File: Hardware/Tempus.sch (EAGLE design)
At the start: 36 parts, among them J7 AVR_SPI_PRG_6NS, U1 ATMEGA328P_TQFP, Y1 16MHZ

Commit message: Hardware modifications
Hardware modifications
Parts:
- removed J1, J10, J11, J12, J13, J14, J15, J17, J18, J19, J2, J20, J21, J22, J23, J24, J25, J3, J4, J5, J6, J8, J9: (no value), SparkFun-Connectors:M01NOSILK-KIT
- removed J16: (no value), SparkFun-Connectors:M06NO_SILK_FEMALE_PTH
- added U$1: DISP_TFT18, KarlVaello-Displays:DISP_TFT18
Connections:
- net A0: no longer J1.1
- net A1: no longer J2.1
- net A2: no longer J3.1
- net A3: no longer J17.1
- net A4: no longer J20.1
- net A5: no longer J21.1
- net A6: no longer J18.1
- net A7: no longer J19.1
- net D10: no longer J6.1
- net D2: no longer J11.1
- net D3: no longer J12.1
- net D4: no longer J13.1
- net D5: no longer J14.1
- net D6: no longer J15.1
- net D7: no longer J8.1
- net D8: no longer J4.1
- net D9: no longer J5.1
- net DTR: no longer J16.1
- net GND: no longer J16.5, J16.6, J24.1, J25.1
- net RXI: no longer J16.3, J9.1
- net TXO: no longer J10.1, J16.2
- net VCC: no longer J16.4, J22.1, J23.1

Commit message: Hardware modifications
Hardware modifications
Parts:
- removed J7: AVR_SPI_PRG_6NS, SparkFun-Connectors:AVR_SPI_PRG_6NS
- added J1: AVR_SPI_PRG_6TESTPOINTS, SparkFun-Connectors:AVR_SPI_PRG_6TESTPOINTS
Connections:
- net GND: now also J1.6; no longer J7.6
- net MISO: now also J1.1; no longer J7.1
- net MOSI: now also J1.4; no longer J7.4
- net RST: now also J1.5; no longer J7.5
- net SCK: now also J1.3; no longer J7.3
- net VCC: now also J1.2; no longer J7.2
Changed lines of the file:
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@@
 <part name="P+5" library="KarlVaello-Simbols" deviceset="VCC" device=""/>
 <part name="S1" library="SparkFun-Retired" deviceset="TAC_SWITCH" device="SMD" value="RESET"/>
-<part name="J7" library="SparkFun-Connectors" deviceset="AVR_SPI_PRG_6" device="NS"/>
 <part name="LED1" library="adafruit" deviceset="LED" device="CHIPLED_0805"/>
 <part name="Y1" library="SparkFun-FreqCtrl" deviceset="RESONATOR" device="16MHZ" value="16MHZ"/>
 <part name="U$1" library="KarlVaello-Displays" deviceset="DISP_TFT18" device=""/>
+<part name="J1" library="SparkFun-Connectors" deviceset="AVR_SPI_PRG_6" device="TESTPOINTS"/>
 </parts>
 <sheets>
@@
 <wire x1="-10.16" y1="60.96" x2="-10.16" y2="38.1" width="0.3048" layer="94" style="shortdash"/>
 <wire x1="-10.16" y1="38.1" x2="-20.32" y2="38.1" width="0.3048" layer="94" style="shortdash"/>
+<wire x1="238.76" y1="-71.12" x2="-88.9" y2="-71.12" width="0.6096" layer="94"/>
 </plain>
 <instances>
@@
 <instance part="P+5" gate="VCC" x="185.42" y="109.22"/>
 <instance part="S1" gate="S" x="50.8" y="86.36" rot="R90"/>
-<instance part="J7" gate="G$1" x="-33.02" y="50.8"/>
 <instance part="LED1" gate="G$1" x="142.24" y="15.24"/>
 <instance part="Y1" gate="G$1" x="88.9" y="66.04" rot="R270"/>
 <instance part="U$1" gate="G$1" x="129.54" y="-38.1"/>
+<instance part="J1" gate="G$1" x="-33.02" y="50.8"/>
 </instances>
 <busses>
@@
 <wire x1="-22.86" y1="48.26" x2="-17.78" y2="48.26" width="0.1524" layer="91"/>
 <label x="-17.78" y="48.26" size="1.27" layer="95" font="vector" ratio="9" xref="yes"/>
-<pinref part="J7" gate="G$1" pin="6"/>
+<pinref part="J1" gate="G$1" pin="6"/>
 </segment>
 <segment>
@@
 <wire x1="-22.86" y1="53.34" x2="-17.78" y2="53.34" width="0.1524" layer="91"/>
 <label x="-17.78" y="53.34" size="1.27" layer="95" font="vector" ratio="9" xref="yes"/>
-<pinref part="J7" gate="G$1" pin="2"/>
+<pinref part="J1" gate="G$1" pin="2"/>
 </segment>
 </net>
@@
 <wire x1="-40.64" y1="50.8" x2="-45.72" y2="50.8" width="0.1524" layer="91"/>
 <label x="-45.72" y="50.8" size="1.27" layer="95" font="vector" ratio="9" rot="R180" xref="yes"/>
-<pinref part="J7" gate="G$1" pin="3"/>
+<pinref part="J1" gate="G$1" pin="3"/>
 </segment>
 </net>
@@
 <wire x1="-22.86" y1="50.8" x2="-17.78" y2="50.8" width="0.1524" layer="91"/>
 <label x="-17.78" y="50.8" size="1.27" layer="95" font="vector" ratio="9" xref="yes"/>
-<pinref part="J7" gate="G$1" pin="4"/>
+<pinref part="J1" gate="G$1" pin="4"/>
 </segment>
 </net>
@@
 <wire x1="-40.64" y1="53.34" x2="-45.72" y2="53.34" width="0.1524" layer="91"/>
 <label x="-45.72" y="53.34" size="1.27" layer="95" font="vector" ratio="9" rot="R180" xref="yes"/>
-<pinref part="J7" gate="G$1" pin="1"/>
+<pinref part="J1" gate="G$1" pin="1"/>
 </segment>
 </net>
@@
 <wire x1="-40.64" y1="48.26" x2="-45.72" y2="48.26" width="0.1524" layer="91"/>
 <label x="-45.72" y="48.26" size="1.27" layer="95" font="vector" ratio="9" rot="R180" xref="yes"/>
-<pinref part="J7" gate="G$1" pin="5"/>
-</segment>
-</net>
+<pinref part="J1" gate="G$1" pin="5"/>
+</segment>
+</net>

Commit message: Hardware
Hardware
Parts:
- removed LED1: (no value), adafruit:LEDCHIPLED_0805
- removed R1, R2, R3: (no value), KarlVaello-Resistors:R-EU_R0805
- added C4: (no value), KarlVaello-Capacitors:C-EUC1608
- added C5, C8: (no value), KarlVaello-Capacitors:CPOL-EUA/3216-18R
- added J2: (no value), SparkFun-Connectors:ARDUINO_SERIAL_PROGRAMPTH
- added R5, R6, R7: (no value), KarlVaello-Resistors:R-EU_R0603
- added U$2, U$3, U$4: MICRO_SIDE_TACT_BUTTON_SMD_SECURE, KarlVaello-ElectroMechanical:MICRO_SIDE_TACT_BUTTON_SMD_SECURE
- added U$5: (no value), bc417:BTM400_6B
- added U2: MIC5205, SparkFun-PowerIC:MIC52055V
- C1, C2, C3: device KarlVaello-Capacitors:C-EUC0805 -> KarlVaello-Capacitors:C-EUC1608
- R4: device KarlVaello-Resistors:R-EU_R0805 -> KarlVaello-Resistors:R-EU_R0603
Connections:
- net RXI renamed D0/RXI
- net TXO renamed D1/TXO
- removed net D10: U1.PB2(SS/OC1B)
- removed net MISO: J1.1, U1.PB4(MISO)
- removed net MOSI: J1.4, U1.PB3(MOSI/OC2)
- removed net N$1: LED1.A, R1.1
- removed net RST: J1.5
- removed net SCK: J1.3, R1.2, U1.PB5(SCK)
- new net D10/SS: U$1.SDA, U1.PB2(SS/OC1B)
- new net D11/MOSI: J1.4, U$1.SCL, U1.PB3(MOSI/OC2)
- new net D12/MISO: J1.1, U$1.CS, U1.PB4(MISO)
- new net D13/SCK: J1.3, U1.PB5(SCK)
- new net LIPO: C5.+, U2.EN, U2.IN
- new net N$11: U$1.NC1
- new net N$12: U$1.NC2
- net A4: no longer R2.1
- net A5: no longer R3.1
- net D2: now also U$5.UART-TX
- net D3: now also U$5.UART-RX
- net D4: now also R5.2, U$4.P$1
- net D5: now also R6.2, U$2.P$1
- net D6: now also R7.2, U$3.P$1
- net D8: now also U$1.RST
- net D9: now also U$1.RS
- net GND: now also C4.1, C5.-, C8.-, R5.1, R6.1, R7.1, U$1.GND1, U$1.GND2, U$1.GND3, U$1.LEDA, U2.GND; no longer LED1.C
- net RESET: now also J1.5
- net VCC: now also C4.2, C8.+, U$1.LEDK, U$1.VCC1, U$1.VCC2, U$2.P$2, U$3.P$2, U$4.P$2, U2.OUT; no longer R2.2, R3.2

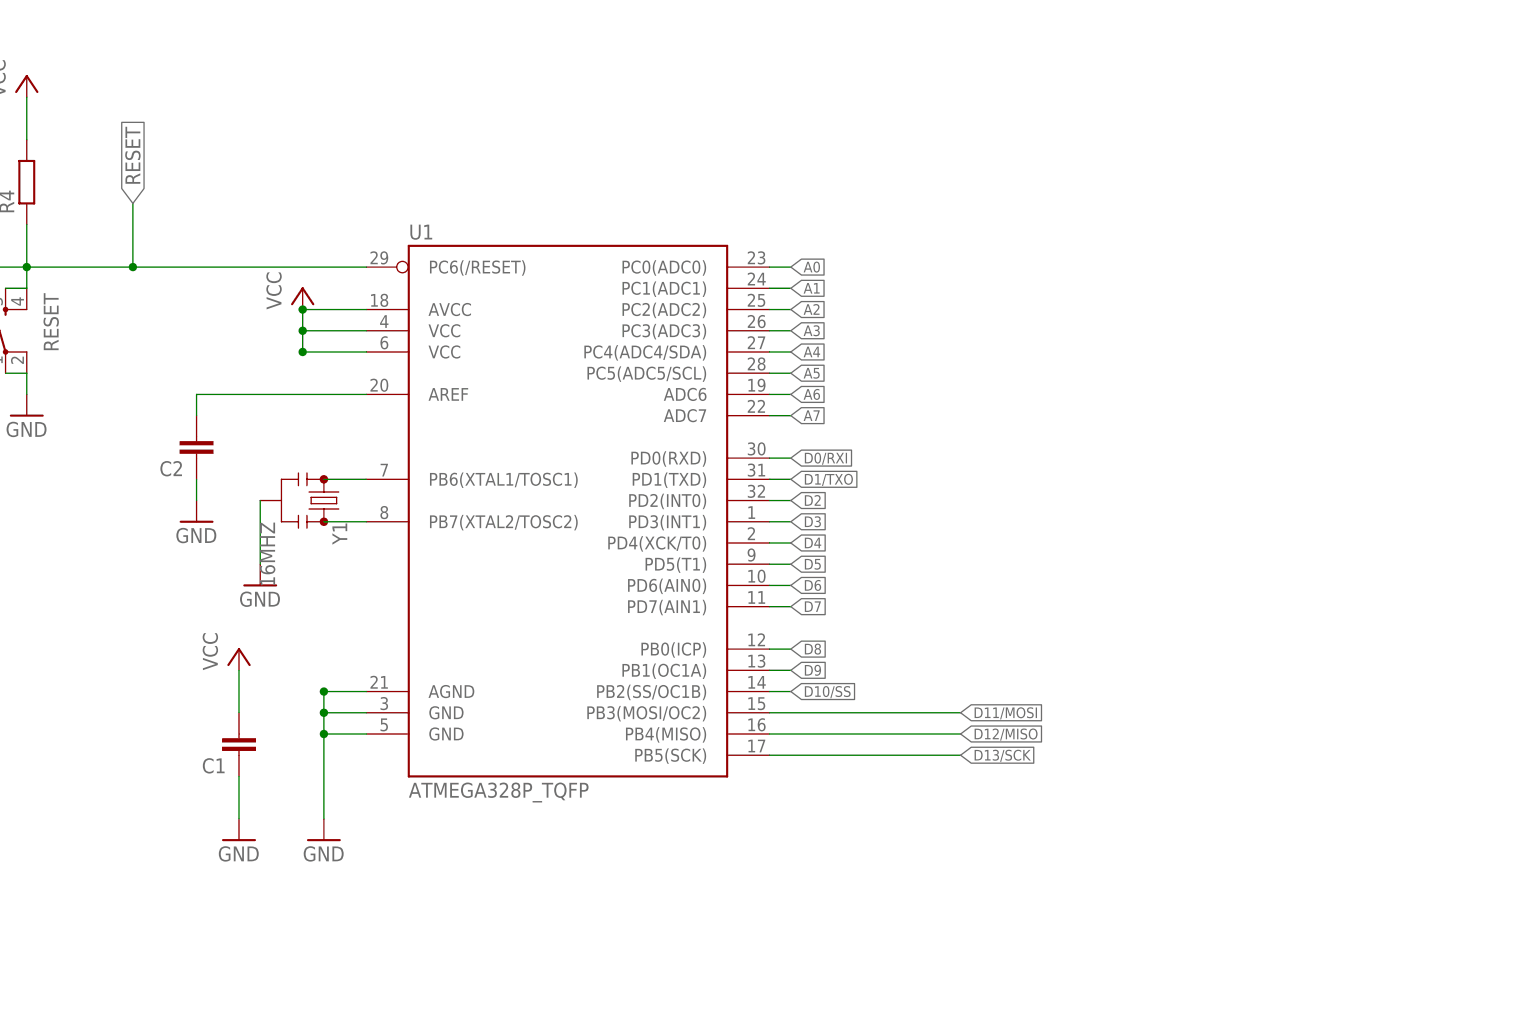
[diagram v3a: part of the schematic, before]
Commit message: Hardware modifications
Hardware modifications. Tempus now based on ARM 32-bit, 3.3V at 48Mhz
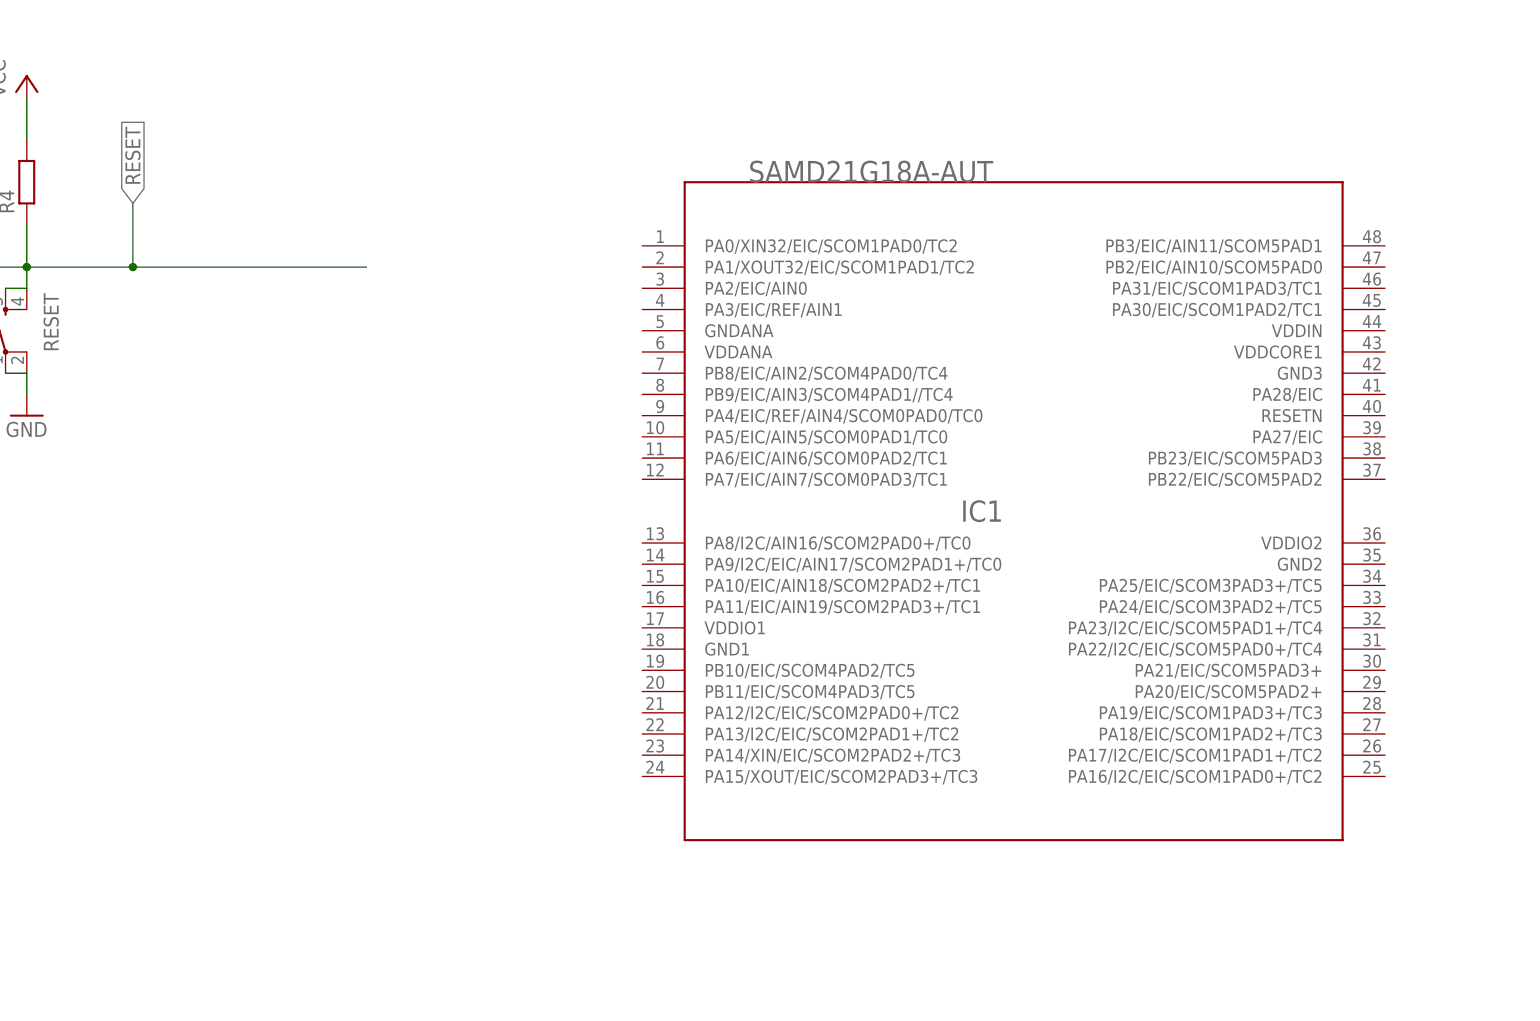
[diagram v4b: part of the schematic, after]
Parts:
- removed C1, C2: (no value), KarlVaello-Capacitors:C-EUC1608
- removed U1: ATMEGA328P_TQFP, KarlVaello-DigitalIC:ATMEGA328P_TQFP
- removed Y1: 16MHZ, SparkFun-FreqCtrl:RESONATOR16MHZ
- added IC1: SAMD21G18A-AUT, KarlVaello-DigitalIC:1792_SAMD21G18A-AUT
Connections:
- removed net A0: U1.PC0(ADC0)
- removed net A1: U1.PC1(ADC1)
- removed net A2: U1.PC2(ADC2)
- removed net A3: U1.PC3(ADC3)
- removed net A4: U1.PC4(ADC4/SDA)
- removed net A5: U1.PC5(ADC5/SCL)
- removed net A6: U1.ADC6
- removed net A7: U1.ADC7
- removed net D0/RXI: U1.PD0(RXD)
- removed net D1/TXO: U1.PD1(TXD)
- removed net D7: U1.PD7(AIN1)
- removed net N$2: U1.PB7(XTAL2/TOSC2), Y1.3
- removed net N$3: C2.2, U1.AREF
- removed net N$6: U1.PB6(XTAL1/TOSC1), Y1.1
- net D10/SS: no longer U1.PB2(SS/OC1B)
- net D11/MOSI: no longer U1.PB3(MOSI/OC2)
- net D12/MISO: no longer U1.PB4(MISO)
- net D13/SCK: no longer U1.PB5(SCK)
- net D2: no longer U1.PD2(INT0)
- net D3: no longer U1.PD3(INT1)
- net D4: no longer U1.PD4(XCK/T0)
- net D5: no longer U1.PD5(T1)
- net D6: no longer U1.PD6(AIN0)
- net D8: no longer U1.PB0(ICP)
- net D9: no longer U1.PB1(OC1A)
- net GND: no longer C1.1, C2.1, U1.AGND, U1.GND@3, U1.GND@5, Y1.2
- net RESET: no longer U1.PC6(/RESET)
- net VCC: no longer C1.2, U1.AVCC, U1.VCC@4, U1.VCC@6
